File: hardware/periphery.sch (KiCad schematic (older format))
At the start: 44 parts, among them J1 JAE_SIM_Card_SF72S006, J11 Micro_SD_Card_Ebay, J2 UART, J3 Bus_PCI_Express_Mini, J8 HR911105_RJ45, SW2 SW_MEC_5G, U2 CH340C, U6 W25Q128JVS or W25N01GV, Y1 24MHz, Y2 32768

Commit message: Translated Russian comments
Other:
- note added: "R18-R21 - possibly DNP"
- note added: "R33-R36 optional?"
- note removed: "R18-R21 - вроде и без них Ethernet работает"
- note removed: "R33-R36 скорее всего не нужны"
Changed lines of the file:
@@
 UART0_RX
 Text Notes 8700 3050 0    50   ~ 0
-R18-R21 - вроде и без них Ethernet работает
+R18-R21 - possibly DNP
 $Comp
 L Device:R R34
@@
 Connection ~ 1400 2750
 Text Notes 2000 1350 0    50   ~ 0
-R33-R36 скорее всего не нужны
+R33-R36 optional?
 Connection ~ 850  1150
 Wire Wire Line

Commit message: Replaced SD card slot with Wurth 693072010801
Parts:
- removed J11: Micro_SD_Card_Ebay, balmer:Conn_uSDcard, symbol balmer_allwinner_v3s_v2-rescue:Micro_SD_Card_Ebay-balmer
- added J11: Micro_SD_Card, Connector_Card:microSD_HC_Wuerth_693072010801, symbol Connector:Micro_SD_Card
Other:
- note added: "Resistors optional?"
- note added: "Termination resistors - possibly DNP"
- note removed: "R18-R21 - possibly DNP"
- note removed: "R33-R36 optional?"
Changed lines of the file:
@@
 Text GLabel 1350 1650 0    50   Input ~ 0
 SDC0_D2
-$Comp
-L balmer_allwinner_v3s_v2-rescue:Micro_SD_Card_Ebay-balmer J11
-U 1 1 5F2C4E0F
-P 2650 2050
-F 0 "J11" H 3480 2050 50  0000 L CNN
-F 1 "Micro_SD_Card_Ebay" H 3480 2050 50  0001 L CNN
-F 2 "balmer:Conn_uSDcard" H 3480 1959 50  0001 L CNN
-F 3 "https://www.hirose.com/product/en/download_file/key_name/DM3/category/Catalog/doc_file_id/49662/?file_category_id=4&item_id=195&is_series=1" H 2650 2150 50  0001 C CNN
-	1    2650 2050
-	1    0    0    -1
-$EndComp
 Text GLabel 1350 1750 0    50   Input ~ 0
 SDC0_D3
@@
 UART0_RX
 Text Notes 8700 3050 0    50   ~ 0
-R18-R21 - possibly DNP
+Termination resistors - possibly DNP
 $Comp
 L Device:R R34
@@
 	1600 2750 1400 2750
 Connection ~ 1400 2750
-Text Notes 2000 1350 0    50   ~ 0
-R33-R36 optional?
+Text Notes 1300 1050 0    50   ~ 0
+Resistors optional?
 Connection ~ 850  1150
 Wire Wire Line
@@
 Text GLabel 4850 4950 0    50   Input ~ 0
 SDC1_CLK
+$Comp
+L Connector:Micro_SD_Card J11
+U 1 1 62362F76
+P 2650 1950
+F 0 "J11" H 2600 2667 50  0000 C CNN
+F 1 "Micro_SD_Card" H 2600 2576 50  0000 C CNN
+F 2 "Connector_Card:microSD_HC_Wuerth_693072010801" H 3800 2250 50  0001 C CNN
+F 3 "http://katalog.we-online.de/em/datasheet/693072010801.pdf" H 2650 1950 50  0001 C CNN
+	1    2650 1950
+	1    0    0    -1
+$EndComp
+$Comp
+L power:GND #PWR0178
+U 1 1 62381551
+P 3450 2550
+F 0 "#PWR0178" H 3450 2300 50  0001 C CNN
+F 1 "GND" H 3455 2377 50  0001 C CNN
+F 2 "" H 3450 2550 50  0001 C CNN
+F 3 "" H 3450 2550 50  0001 C CNN
+	1    3450 2550
+	0    -1   -1   0
+$EndComp
 $EndSCHEMATC

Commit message: Some routing improvements
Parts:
- C25, C26, C28, C29: value 18 -> 18p
- R14, R15: value 1K -> 200R
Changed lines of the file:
@@
 P 10500 1050
 F 0 "C26" H 10615 1096 50  0000 L CNN
-F 1 "18" H 10615 1005 50  0000 L CNN
+F 1 "18p" H 10615 1005 50  0000 L CNN
 F 2 "Capacitor_SMD:C_0603_1608Metric" H 10538 900 50  0001 C CNN
 F 3 "~" H 10500 1050 50  0001 C CNN
@@
 P 9850 1050
 F 0 "C25" H 9965 1096 50  0000 L CNN
-F 1 "18" H 9965 1005 50  0000 L CNN
+F 1 "18p" H 9965 1005 50  0000 L CNN
 F 2 "Capacitor_SMD:C_0603_1608Metric" H 9888 900 50  0001 C CNN
 F 3 "~" H 9850 1050 50  0001 C CNN
@@
 P 9900 2150
 F 0 "C28" H 10015 2196 50  0000 L CNN
-F 1 "18" H 10015 2105 50  0000 L CNN
+F 1 "18p" H 10015 2105 50  0000 L CNN
 F 2 "Capacitor_SMD:C_0603_1608Metric" H 9938 2000 50  0001 C CNN
 F 3 "~" H 9900 2150 50  0001 C CNN
@@
 P 10450 2150
 F 0 "C29" H 10565 2196 50  0000 L CNN
-F 1 "18" H 10565 2105 50  0000 L CNN
+F 1 "18p" H 10565 2105 50  0000 L CNN
 F 2 "Capacitor_SMD:C_0603_1608Metric" H 10488 2000 50  0001 C CNN
 F 3 "~" H 10450 2150 50  0001 C CNN
@@
 P 8900 3200
 F 0 "R14" V 8800 3200 50  0000 C CNN
-F 1 "1K" V 8900 3200 50  0000 C CNN
+F 1 "200R" V 8900 3200 50  0000 C CNN
 F 2 "Resistor_SMD:R_0603_1608Metric" V 8830 3200 50  0001 C CNN
 F 3 "~" H 8900 3200 50  0001 C CNN
@@
 P 8900 3400
 F 0 "R15" V 8800 3400 50  0000 C CNN
-F 1 "1K" V 8900 3400 50  0000 C CNN
+F 1 "200R" V 8900 3400 50  0000 C CNN
 F 2 "Resistor_SMD:R_0603_1608Metric" V 8830 3400 50  0001 C CNN
 F 3 "~" H 8900 3400 50  0001 C CNN

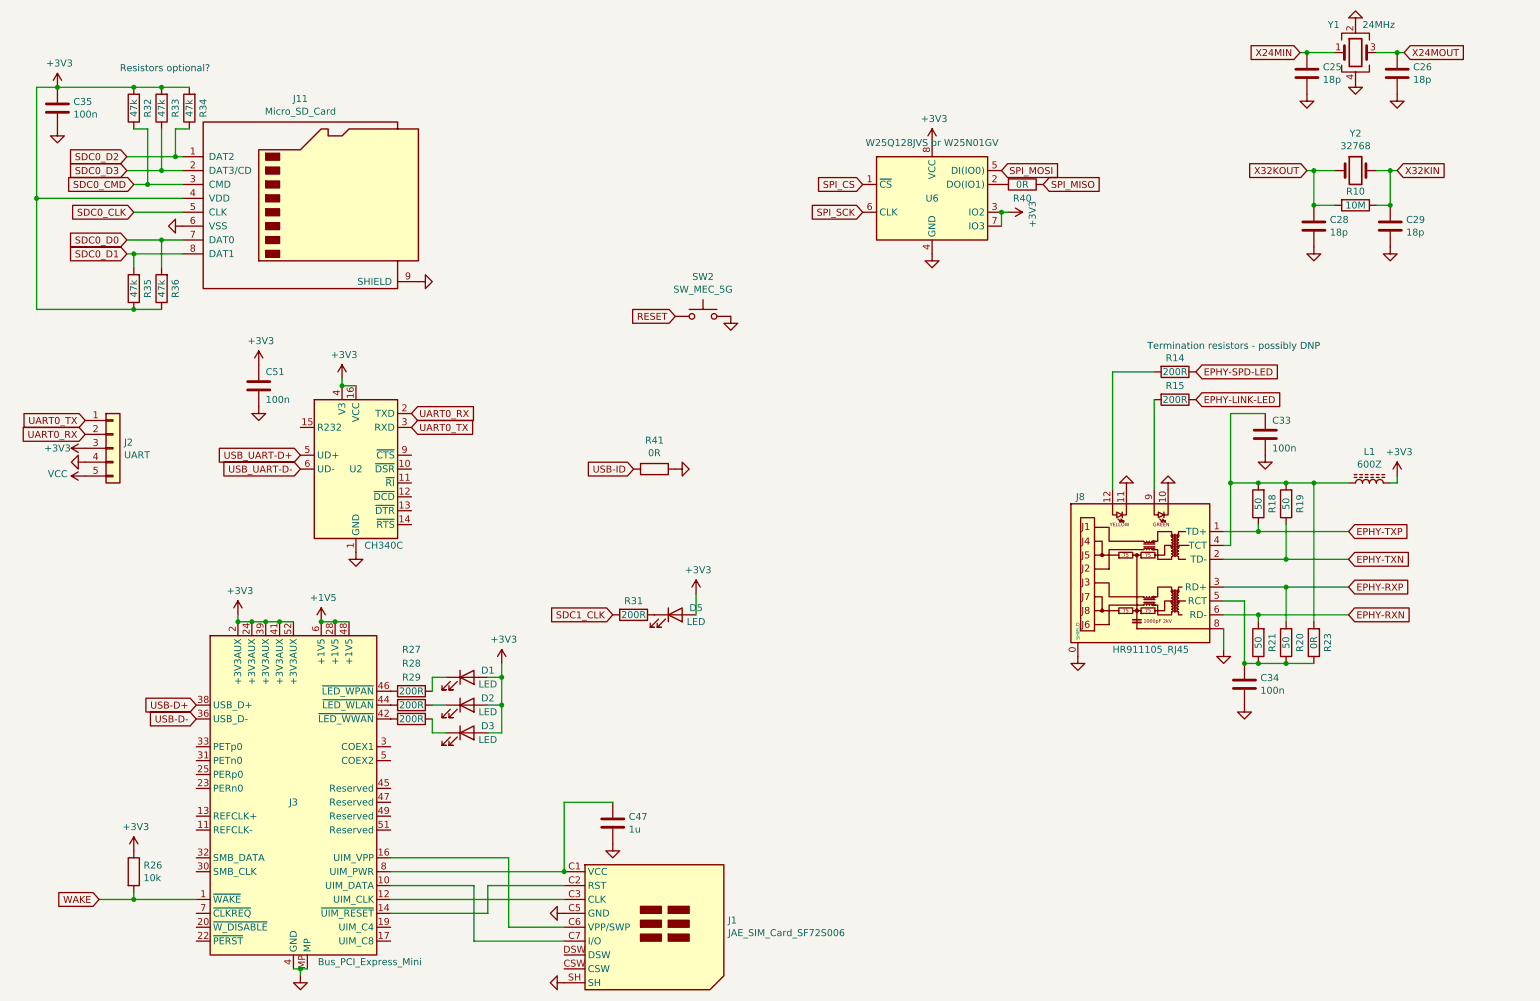
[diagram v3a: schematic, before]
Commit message: Move Y1 to top-layer
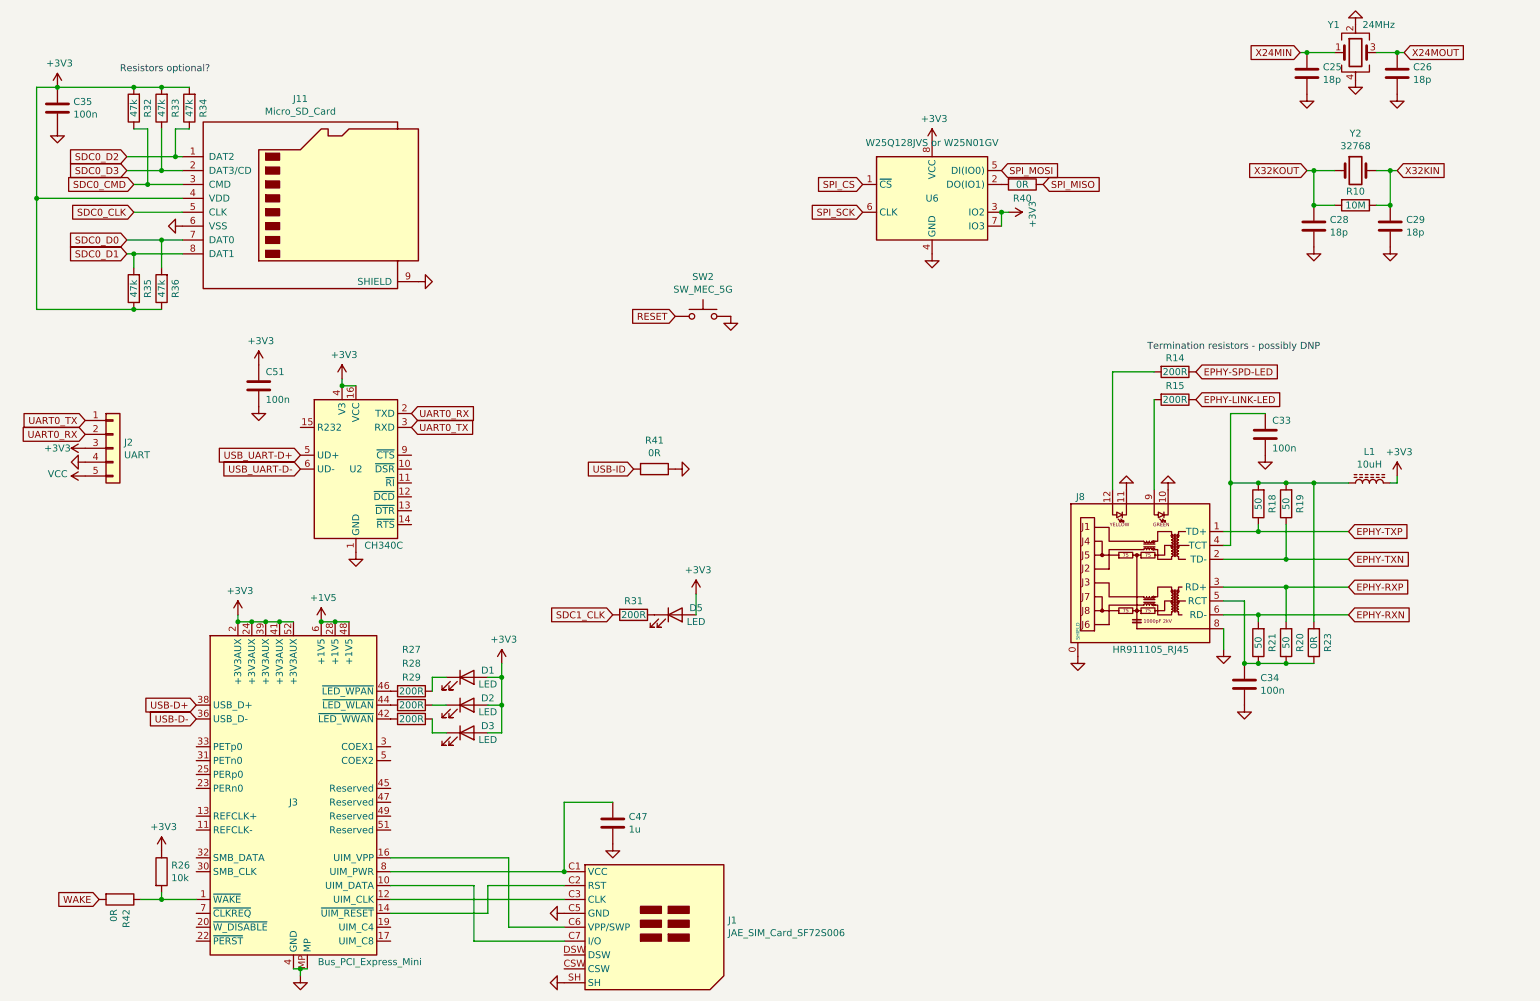
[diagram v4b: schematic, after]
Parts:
- added R42: 0R, Resistor_SMD:R_0603_1608Metric, symbol Device:R
- L1: value 600Z -> 10uH
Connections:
- net WAKE: now also R42.2; no longer J3.1 (~WAKE), R26.2
- new net: J3.1 (~WAKE), R26.2, R42.1
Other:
- moved on the sheet: R26
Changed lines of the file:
@@
 P 10300 4000
 F 0 "L1" V 10525 4000 50  0000 C CNN
-F 1 "600Z" V 10434 4000 50  0000 C CNN
+F 1 "10uH" V 10434 4000 50  0000 C CNN
 F 2 "Inductor_SMD:L_1206_3216Metric" H 10300 4000 50  0001 C CNN
 F 3 "~" H 10300 4000 50  0001 C CNN
@@
 L Device:R R26
 U 1 1 6279758E
-P 1400 6800
-F 0 "R26" H 1470 6846 50  0000 L CNN
-F 1 "10k" H 1470 6755 50  0000 L CNN
-F 2 "Resistor_SMD:R_0603_1608Metric" V 1330 6800 50  0001 C CNN
-F 3 "~" H 1400 6800 50  0001 C CNN
-	1    1400 6800
+P 1600 6800
+F 0 "R26" H 1670 6846 50  0000 L CNN
+F 1 "10k" H 1670 6755 50  0000 L CNN
+F 2 "Resistor_SMD:R_0603_1608Metric" V 1530 6800 50  0001 C CNN
+F 3 "~" H 1600 6800 50  0001 C CNN
+	1    1600 6800
 	1    0    0    -1
 $EndComp
@@
 L power:+3V3 #PWR019
 U 1 1 627982F2
-P 1400 6650
-F 0 "#PWR019" H 1400 6500 50  0001 C CNN
-F 1 "+3V3" H 1415 6823 50  0000 C CNN
-F 2 "" H 1400 6650 50  0001 C CNN
-F 3 "" H 1400 6650 50  0001 C CNN
-	1    1400 6650
-	1    0    0    -1
-$EndComp
-Wire Wire Line
-	1400 7000 1400 6950
+P 1600 6650
+F 0 "#PWR019" H 1600 6500 50  0001 C CNN
+F 1 "+3V3" H 1615 6823 50  0000 C CNN
+F 2 "" H 1600 6650 50  0001 C CNN
+F 3 "" H 1600 6650 50  0001 C CNN
+	1    1600 6650
+	1    0    0    -1
+$EndComp
 Text GLabel 1150 7000 0    50   Input ~ 0
 WAKE
-Wire Wire Line
-	1150 7000 1400 7000
-Connection ~ 1400 7000
-Wire Wire Line
-	1400 7000 1850 7000
 $Comp
 L power:VCC #PWR0176
@@
 	0    -1   -1   0
 $EndComp
+Wire Wire Line
+	1600 6950 1600 7000
+Wire Wire Line
+	1600 7000 1850 7000
+$Comp
+L Device:R R42
+U 1 1 6249164C
+P 1300 7000
+F 0 "R42" H 1370 7046 50  0000 L CNN
+F 1 "0R" H 1370 6955 50  0000 L CNN
+F 2 "Resistor_SMD:R_0603_1608Metric" V 1230 7000 50  0001 C CNN
+F 3 "~" H 1300 7000 50  0001 C CNN
+	1    1300 7000
+	0    1    1    0
+$EndComp
+Wire Wire Line
+	1450 7000 1600 7000
+Connection ~ 1600 7000
 $EndSCHEMATC

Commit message: Fixed filenames
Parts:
- J8: footprint balmer:HR911105_RJ45 -> moonpi:HR911105_RJ45; symbol balmer_allwinner_v3s_v2-rescue:HR911105_RJ45-hr911105_rj45 -> moonpi_v2-rescue:HR911105_RJ45-hr911105_rj45
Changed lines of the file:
@@
 EPHY-RXN
 $Comp
-L balmer_allwinner_v3s_v2-rescue:HR911105_RJ45-hr911105_rj45 J8
+L moonpi_v2-rescue:HR911105_RJ45-hr911105_rj45 J8
 U 1 1 5F20EFFF
 P 8650 4650
 F 0 "J8" H 8250 5200 50  0000 R CNN
 F 1 "HR911105_RJ45" H 9000 4100 50  0000 R CNN
-F 2 "balmer:HR911105_RJ45" H 8650 4025 50  0001 C CNN
+F 2 "moonpi:HR911105_RJ45" H 8650 4025 50  0001 C CNN
 F 3 "HR911105_RJ45" H 8235 4415 50  0001 L TNN
 	1    8650 4650

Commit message: Fixed filename verioning
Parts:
- J8: symbol moonpi_v2-rescue:HR911105_RJ45-hr911105_rj45 -> moonpi-rescue:HR911105_RJ45-hr911105_rj45
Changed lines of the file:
@@
 EPHY-RXN
 $Comp
-L moonpi_v2-rescue:HR911105_RJ45-hr911105_rj45 J8
+L moonpi-rescue:HR911105_RJ45-hr911105_rj45 J8
 U 1 1 5F20EFFF
 P 8650 4650

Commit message: FIX: Added pull-up on SPI /CS
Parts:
- added R43: 10k, Resistor_SMD:R_0603_1608Metric, symbol Device:R
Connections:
- net +3V3: now also R43.2
- net SPI_CS: now also R43.1
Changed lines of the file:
@@
 	9900 4000 10150 4000
 Connection ~ 9400 5300
-Text GLabel 6650 1850 0    50   Input ~ 0
+Text GLabel 6150 1850 0    50   Input ~ 0
 SPI_CS
 Text GLabel 6650 2050 0    50   Input ~ 0
@@
 	1450 7000 1600 7000
 Connection ~ 1600 7000
+$Comp
+L Device:R R43
+U 1 1 628236EB
+P 6400 1700
+F 0 "R43" V 6500 1700 50  0000 C CNN
+F 1 "10k" V 6400 1700 50  0000 C CNN
+F 2 "Resistor_SMD:R_0603_1608Metric" V 6330 1700 50  0001 C CNN
+F 3 "~" H 6400 1700 50  0001 C CNN
+	1    6400 1700
+	-1   0    0    1
+$EndComp
+Wire Wire Line
+	6150 1850 6400 1850
+Connection ~ 6400 1850
+Wire Wire Line
+	6400 1850 6650 1850
+$Comp
+L power:+3V3 #PWR031
+U 1 1 6282849A
+P 6400 1550
+F 0 "#PWR031" H 6400 1400 50  0001 C CNN
+F 1 "+3V3" H 6415 1723 50  0000 C CNN
+F 2 "" H 6400 1550 50  0001 C CNN
+F 3 "" H 6400 1550 50  0001 C CNN
+	1    6400 1550
+	1    0    0    -1
+$EndComp
 $EndSCHEMATC
